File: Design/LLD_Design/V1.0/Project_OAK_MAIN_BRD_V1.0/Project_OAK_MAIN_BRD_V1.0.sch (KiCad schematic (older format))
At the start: 98 parts, among them U1 ATmega328PB-MU, U2 RV-8263-C7-32.768KHZ-20PPM-TA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, U3 LIS2DW12TR

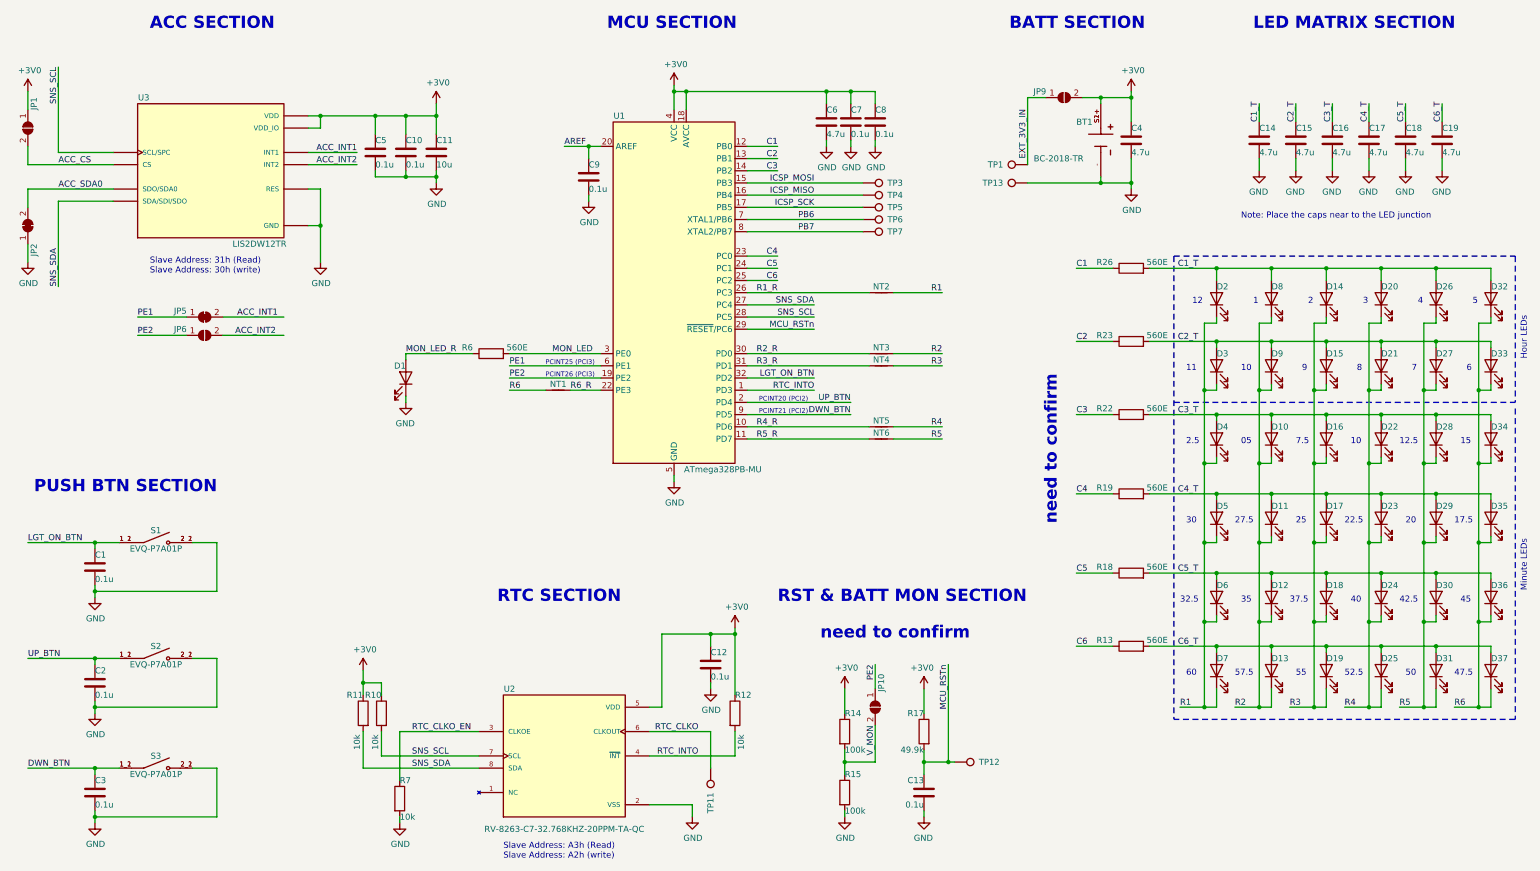
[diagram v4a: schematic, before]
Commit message: SCH update in progress with ACCL sensor change & haptic sensor addition
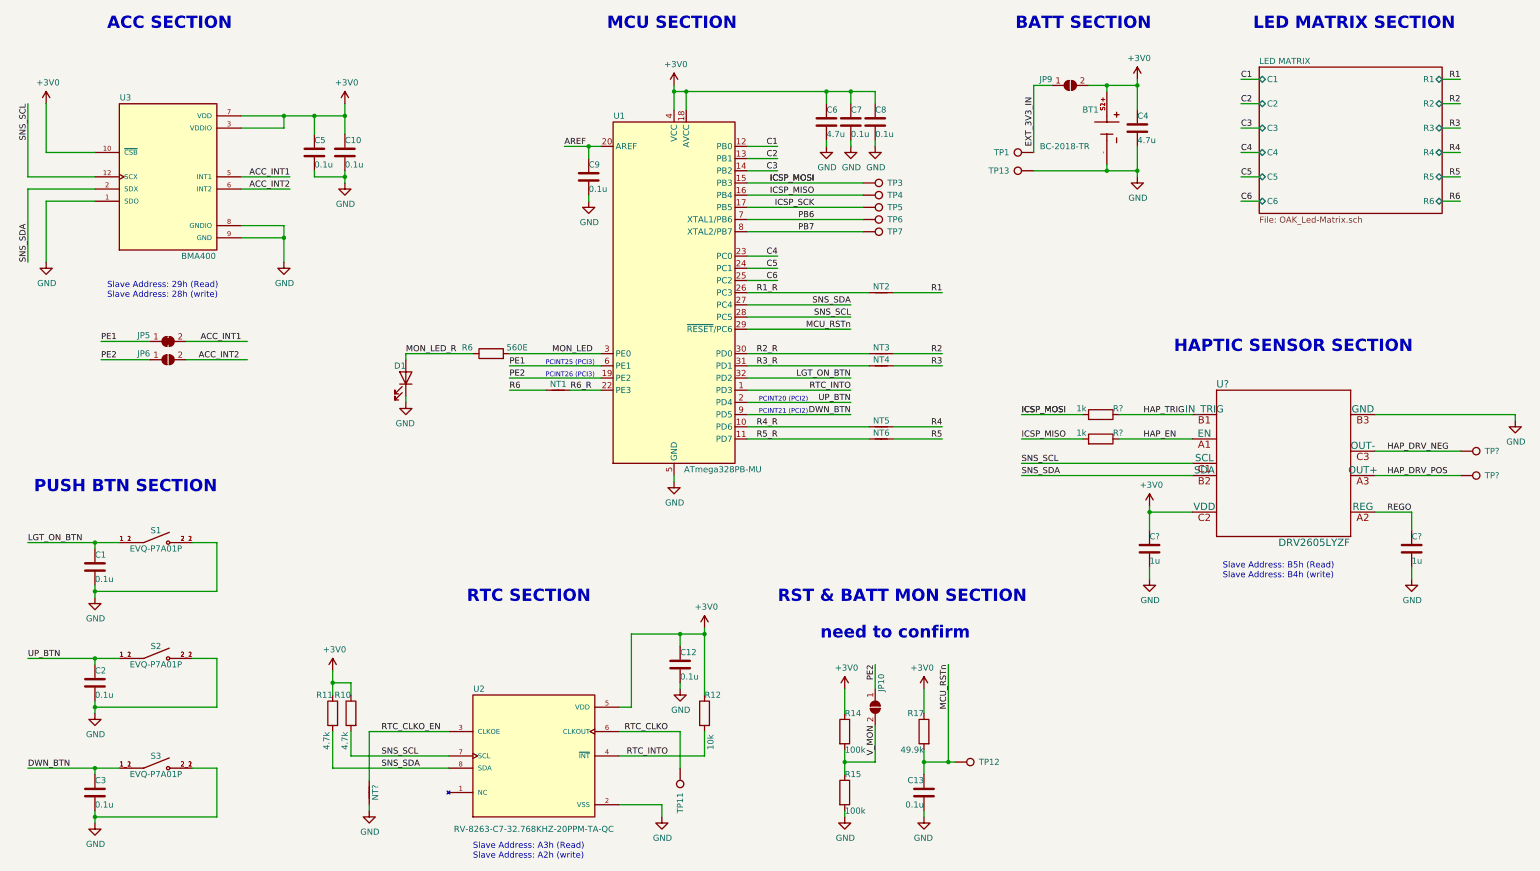
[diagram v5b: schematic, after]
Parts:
- removed C11: 10u, Capacitor_SMD:C_0402_1005Metric, symbol Device:C
- removed C14, C15, C16, C17, C18, C19: 4.7u, Capacitor_SMD:C_0402_1005Metric, symbol Device:C
- removed D10, D11, D12, D13, D14, D15, D16, D17, D18, D19, D2, D20, D21, D22, D23, D24, D25, D26, D27, D28, D29, D3, D30, D31, D32, D33, D34, D35, D36, D37, D4, D5, D6, D7, D8, D9: LED, LED_SMD:LED_0402_1005Metric, symbol Device:LED
- removed JP1: SolderJumper_2_Open, Jumper:SolderJumper-2_Open_Pad1.0x1.5mm_custom, symbol Jumper:SolderJumper_2_Open
- removed JP2: SolderJumper_2_Bridged, Jumper:SolderJumper-2_Bridged_Pad1.0x1.5mm_custom, symbol Jumper:SolderJumper_2_Bridged
- removed R13, R18, R19, R22, R23, R26: 560E, Resistor_SMD:R_0402_1005Metric, symbol Device:R
- removed R7: 10k, Resistor_SMD:R_0402_1005Metric, symbol Device:R
- removed U3: LIS2DW12TR, Sensor:LIS2DW12TR, symbol LIS2DW12TR:LIS2DW12TR
- added C? (x2): 1u, Capacitor_SMD:C_0402_1005Metric, symbol Device:C
- added NT?: Net-Tie_2, NetTie:NetTie-2_SMD_Custom, symbol Device:Net-Tie_2
- added R? (x2): 1k, Resistor_SMD:R_0402_1005Metric, symbol Device:R
- added TP? (x2): TestPoint, TestPoint:TestPoint_Pad_D1.0mm, symbol Connector:TestPoint
- added U3: BMA400, XDCR_BMA400, symbol BMA400:BMA400
- added U?: DRV2605LYZF, YZF0009ADAD, symbol DRV2605LYZFR:DRV2605LYZF
- R10, R11: value 10k -> 4.7k
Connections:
- net +3V0: now also C?.1, U3.10 (~CSB), U3.3 (VDDIO), U3.7 (VDD), U?.C2 (VDD)
- net ACC_INT1: now also U3.5 (INT1)
- net ACC_INT2: now also U3.6 (INT2)
- net GND: now also C?.2, C?.2, NT?.2, U3.1 (SDO), U3.8 (GNDIO), U3.9 (GND), U?.B3 (GND)
- net ICSP_MISO: now also R?.2
- net ICSP_MOSI: now also R?.2
- net RTC_CLKO_EN: now also NT?.1
- net SNS_SCL: now also U3.12 (SCX), U?.C1 (SCL)
- net SNS_SDA: now also U3.2 (SDX), U?.B2 (SDA)
- new net HAP_DRV_NEG: TP?.1, U?.C3 (OUT-)
- new net HAP_DRV_POS: TP?.1, U?.A3 (OUT+)
- new net HAP_EN: R?.1, U?.A1 (EN)
- new net HAP_TRIG: R?.1, U?.B1 (IN_TRIG)
- new net REGO: C?.1, U?.A2 (REG)
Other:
- note added: "HAPTIC SENSOR SECTION"
- note added: "Slave Address: 29h (Read)\nSlave Address: 28h (write)"
- note added: "Slave Address: B5h (Read)\nSlave Address: B4h (write)"
- note removed: "05"
- note removed: "1"
- note removed: "10"
- note removed: "11"
- note removed: "12"
- note removed: "12.5"
- note removed: "15"
- note removed: "17.5"
- note removed: "2"
- note removed: "2.5"
- note removed: "20"
- note removed: "22.5"
- note removed: "25"
- note removed: "27.5"
- note removed: "3"
- note removed: "30"
- note removed: "32.5"
- note removed: "35"
- note removed: "37.5"
- note removed: "4"
- note removed: "40"
- note removed: "42.5"
- note removed: "45"
- note removed: "47.5"
- note removed: "5"
- note removed: "50"
- note removed: "52.5"
- note removed: "55"
- note removed: "57.5"
- note removed: "6"
- note removed: "60"
- note removed: "7"
- note removed: "7.5"
- note removed: "8"
- note removed: "9"
- note removed: "Hour LEDs"
- note removed: "Minute LEDs"
- note removed: "Note: Place the caps near to the LED junction"
- note removed: "Slave Address: 31h (Read)\nSlave Address: 30h (write)"
- moved on the sheet: BT1, C10, C12, C4, C5, JP5, JP6, JP9, R10, R11, R12, TP1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

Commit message: layout update in progress
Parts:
- added R3: 100k, Resistor_SMD:R_0402_1005Metric, symbol Device:R
- U3: footprint XDCR_BMA400 -> Sensor:BMA400
- U4: renamed from U?; footprint YZF0009ADAD -> Sensor:DRV2605LYZFR
- gave numbers to parts that had none: 7
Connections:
- net +3V0: now also R3.1
- net HAP_EN: now also R3.2
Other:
- note added: "DNP"
- moved on the sheet: C11, C20, R1, R2, TP2, TP8, U4
